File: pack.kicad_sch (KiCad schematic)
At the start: 37 parts, among them Q1 AON7544, Q2 AO3401A, Q3 AON7544, U1 BQ40z50-R2

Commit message: Fix swapped gauage current sense pins
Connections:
- net GND: now also R2.1; no longer R3.2
- net GND1: now also R3.1; no longer R2.2
- net PS+: now also R3.2; no longer R3.1
- net PS-: now also R2.2; no longer R2.1
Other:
- moved on the sheet: C2, C5, R2, R3
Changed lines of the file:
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@@
+    (stroke (width 0) (type default) (color 0 0 0 0))
+  )
+  (wire (pts (xy 87.63 132.08) (xy 104.14 132.08))
     (stroke (width 0) (type default) (color 0 0 0 0))
   )
@@
     (stroke (width 0) (type default) (color 0 0 0 0))
   )
+  (wire (pts (xy 107.95 119.38) (xy 107.95 124.46))
+    (stroke (width 0) (type default) (color 0 0 0 0))
+  )
   (wire (pts (xy 173.99 62.23) (xy 175.26 62.23))
     (stroke (width 0) (type default) (color 0 0 0 0))
@@
     (stroke (width 0) (type default) (color 0 0 0 0))
   )
-  (wire (pts (xy 97.79 124.46) (xy 104.14 124.46))
-    (stroke (width 0) (type default) (color 0 0 0 0))
-  )
-  (wire (pts (xy 87.63 132.08) (xy 107.95 132.08))
-    (stroke (width 0) (type default) (color 0 0 0 0))
-  )
   (wire (pts (xy 130.81 62.23) (xy 144.78 62.23))
     (stroke (width 0) (type default) (color 0 0 0 0))
@@
     (stroke (width 0) (type default) (color 0 0 0 0))
   )
-  (wire (pts (xy 107.95 132.08) (xy 107.95 119.38))
-    (stroke (width 0) (type default) (color 0 0 0 0))
-  )
   (wire (pts (xy 175.26 96.52) (xy 175.26 92.71))
     (stroke (width 0) (type default) (color 0 0 0 0))
@@
     (stroke (width 0) (type default) (color 0 0 0 0))
   )
-  (wire (pts (xy 104.14 124.46) (xy 104.14 111.76))
+  (wire (pts (xy 104.14 132.08) (xy 104.14 111.76))
     (stroke (width 0) (type default) (color 0 0 0 0))
   )
@@
   )
   (wire (pts (xy 119.38 71.12) (xy 125.73 71.12))
+    (stroke (width 0) (type default) (color 0 0 0 0))
+  )
+  (wire (pts (xy 97.79 124.46) (xy 107.95 124.46))
     (stroke (width 0) (type default) (color 0 0 0 0))
   )
@@
     (pin "2")
   )
-  (symbol (lib_id "Device:C_Small") (at 97.79 135.89 0) (unit 1)
+  (symbol (lib_id "Device:C_Small") (at 87.63 135.89 0) (unit 1)
     (in_bom yes) (on_board yes)
-    (property "Reference" "C5" (id 0) (at 103.0519 135.8963 90))
-    (property "Value" "100nF" (id 1) (at 100.515 135.8963 90))
-    (property "Footprint" "Capacitor_SMD:C_0402_1005Metric" (id 2) (at 97.79 135.89 0)
-      (effects (font (size 1.27 1.27)) hide)
-    )
-    (property "Datasheet" "~" (id 3) (at 97.79 135.89 0)
-      (effects (font (size 1.27 1.27)) hide)
-    )
-    (property "LCSC" "C1525" (id 4) (at 97.79 135.89 0)
+    (property "Reference" "C5" (id 0) (at 92.8919 135.8963 90))
+    (property "Value" "100nF" (id 1) (at 90.355 135.8963 90))
+    (property "Footprint" "Capacitor_SMD:C_0402_1005Metric" (id 2) (at 87.63 135.89 0)
+      (effects (font (size 1.27 1.27)) hide)
+    )
+    (property "Datasheet" "~" (id 3) (at 87.63 135.89 0)
+      (effects (font (size 1.27 1.27)) hide)
+    )
+    (property "LCSC" "C1525" (id 4) (at 87.63 135.89 0)
       (effects (font (size 1.27 1.27)) hide)
     )
@@
     (pin "1")
   )
-  (symbol (lib_id "Device:R_Small") (at 81.28 124.46 270) (unit 1)
+  (symbol (lib_id "Device:R_Small") (at 81.28 132.08 90) (unit 1)
     (in_bom yes) (on_board yes)
-    (property "Reference" "R2" (id 0) (at 81.28 120.65 90))
-    (property "Value" "100R" (id 1) (at 81.28 122.5605 90))
-    (property "Footprint" "Resistor_SMD:R_0402_1005Metric" (id 2) (at 81.28 124.46 0)
-      (effects (font (size 1.27 1.27)) hide)
-    )
-    (property "Datasheet" "~" (id 3) (at 81.28 124.46 0)
-      (effects (font (size 1.27 1.27)) hide)
-    )
-    (property "LCSC" "C25076" (id 4) (at 81.28 124.46 0)
+    (property "Reference" "R2" (id 0) (at 81.28 135.89 90))
+    (property "Value" "100R" (id 1) (at 81.28 133.9795 90))
+    (property "Footprint" "Resistor_SMD:R_0402_1005Metric" (id 2) (at 81.28 132.08 0)
+      (effects (font (size 1.27 1.27)) hide)
+    )
+    (property "Datasheet" "~" (id 3) (at 81.28 132.08 0)
+      (effects (font (size 1.27 1.27)) hide)
+    )
+    (property "LCSC" "C25076" (id 4) (at 81.28 132.08 0)
       (effects (font (size 1.27 1.27)) hide)
     )
@@
     (pin "2")
   )
-  (symbol (lib_id "Device:R_Small") (at 81.28 132.08 270) (unit 1)
+  (symbol (lib_id "Device:R_Small") (at 81.28 124.46 90) (unit 1)
     (in_bom yes) (on_board yes)
-    (property "Reference" "R3" (id 0) (at 81.28 134.62 90))
-    (property "Value" "100R" (id 1) (at 81.28 137.16 90))
-    (property "Footprint" "Resistor_SMD:R_0402_1005Metric" (id 2) (at 81.28 132.08 0)
-      (effects (font (size 1.27 1.27)) hide)
-    )
-    (property "Datasheet" "~" (id 3) (at 81.28 132.08 0)
-      (effects (font (size 1.27 1.27)) hide)
-    )
-    (property "LCSC" "C25076" (id 4) (at 81.28 132.08 0)
+    (property "Reference" "R3" (id 0) (at 81.28 121.92 90))
+    (property "Value" "100R" (id 1) (at 81.28 119.38 90))
+    (property "Footprint" "Resistor_SMD:R_0402_1005Metric" (id 2) (at 81.28 124.46 0)
+      (effects (font (size 1.27 1.27)) hide)
+    )
+    (property "Datasheet" "~" (id 3) (at 81.28 124.46 0)
+      (effects (font (size 1.27 1.27)) hide)
+    )
+    (property "LCSC" "C25076" (id 4) (at 81.28 124.46 0)
       (effects (font (size 1.27 1.27)) hide)
     )
@@
     (pin "1")
   )
-  (symbol (lib_id "Device:C_Small") (at 87.63 135.89 0) (unit 1)
-    (in_bom yes) (on_board yes) (fields_autoplaced)
-    (property "Reference" "C2" (id 0) (at 89.9541 135.0616 0)
-      (effects (font (size 1.27 1.27)) (justify left))
-    )
-    (property "Value" "100nF" (id 1) (at 89.9541 137.5985 0)
-      (effects (font (size 1.27 1.27)) (justify left))
-    )
-    (property "Footprint" "Capacitor_SMD:C_0402_1005Metric" (id 2) (at 87.63 135.89 0)
-      (effects (font (size 1.27 1.27)) hide)
-    )
-    (property "Datasheet" "~" (id 3) (at 87.63 135.89 0)
-      (effects (font (size 1.27 1.27)) hide)
-    )
-    (property "LCSC" "C1525" (id 4) (at 87.63 135.89 0)
+  (symbol (lib_id "Device:C_Small") (at 97.79 135.89 0) (unit 1)
+    (in_bom yes) (on_board yes) (fields_autoplaced)
+    (property "Reference" "C2" (id 0) (at 100.1141 135.0616 0)
+      (effects (font (size 1.27 1.27)) (justify left))
+    )
+    (property "Value" "100nF" (id 1) (at 100.1141 137.5985 0)
+      (effects (font (size 1.27 1.27)) (justify left))
+    )
+    (property "Footprint" "Capacitor_SMD:C_0402_1005Metric" (id 2) (at 97.79 135.89 0)
+      (effects (font (size 1.27 1.27)) hide)
+    )
+    (property "Datasheet" "~" (id 3) (at 97.79 135.89 0)
+      (effects (font (size 1.27 1.27)) hide)
+    )
+    (property "LCSC" "C1525" (id 4) (at 97.79 135.89 0)
       (effects (font (size 1.27 1.27)) hide)
     )
@@
     (pin "1")
   )
-  (symbol (lib_id "Device:C_Small") (at 87.63 128.27 0) (mirror x) (unit 1)
+  (symbol (lib_id "Device:C_Small") (at 87.63 128.27 0) (unit 1)
     (in_bom yes) (on_board yes)
-    (property "Reference" "C1" (id 0) (at 89.9541 129.0984 0)
-      (effects (font (size 1.27 1.27)) (justify left))
-    )
-    (property "Value" "100nF" (id 1) (at 89.9541 126.5615 0)
-      (effects (font (size 1.27 1.27)) (justify left))
-    )
+    (property "Reference" "C1" (id 0) (at 89.9541 127.4416 0)
+      (effects (font (size 1.27 1.27)) (justify left))
+    )
+    (property "Value" "100nF" (id 1) (at 89.9541 129.9785 0)
+      (effects (font (size 1.27 1.27)) (justify left))
+    )

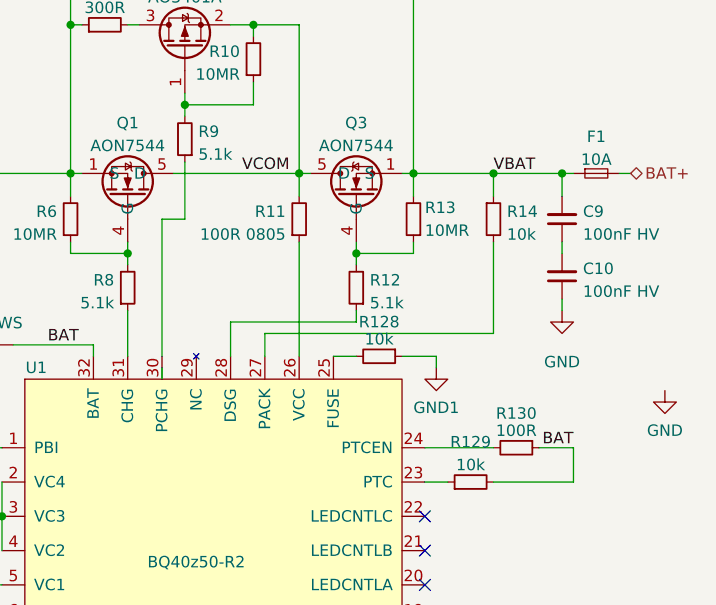
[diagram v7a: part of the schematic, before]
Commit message: Fix remaining RevB bugs
 - DNP Q13 by default to ensure uninterrupted power power delivery
 - Use lower resistance load resistors for DC step-up selftest
 - Add edge rails to support JLCPCB standard assembly

Unfortuantely JLCPCB does not seems to offer ESP32 WROOMs anymore for
economic PCBA. Thus edge-rails have been added to support standard PCBA.
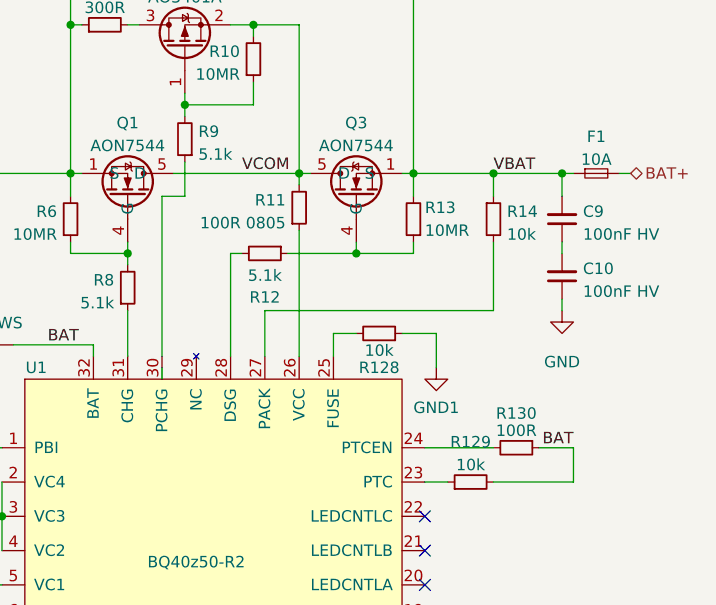
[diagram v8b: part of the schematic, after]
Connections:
- net at U1.28 (DSG): now also R12.2; no longer R12.1
- net at Q3.4 (G), R13.1: now also R12.1; no longer R12.2
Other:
- moved on the sheet: R11, R12, R128
